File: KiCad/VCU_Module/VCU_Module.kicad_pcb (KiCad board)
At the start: 4 copper layers, 85.2 x 107.8 mm, 66 parts, among them IC1 STM32C092RCT6, J1 5810132011, J10 12V, J11 Conn_ST_STDC14, J12 MCU1, J13 MCU2, J14 5V, J15 3V3, J16 MCU3, J17 MCU4, J2 CN1, J3 CN2, J4 CN3, J5 MCU6, J6 CN4, J7 MCU5, J8 Termination Resistor Jumper, J9 GND, Q1 SUD19P06-60, SW2 SW_Push, U3 LMR33640DDDA, U4 LMR33640DDDA, U6 MCP2562FDT-H_SN

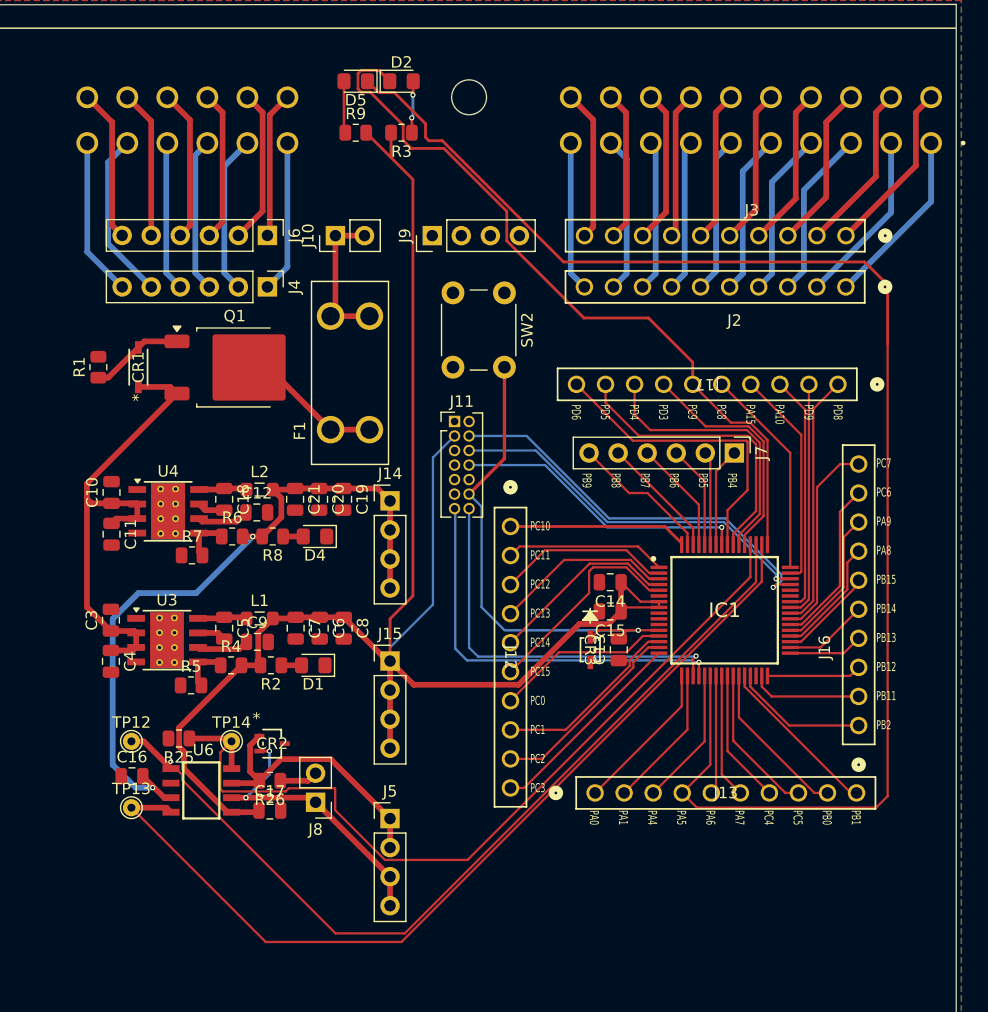
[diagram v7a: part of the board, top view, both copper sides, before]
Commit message: finished DRC checks and ERC checks in schematic and PCB, added many new components with purchase links to BOM, still need to double check previously added parts in BOM to ensure they are sufficient for higher voltage inputs
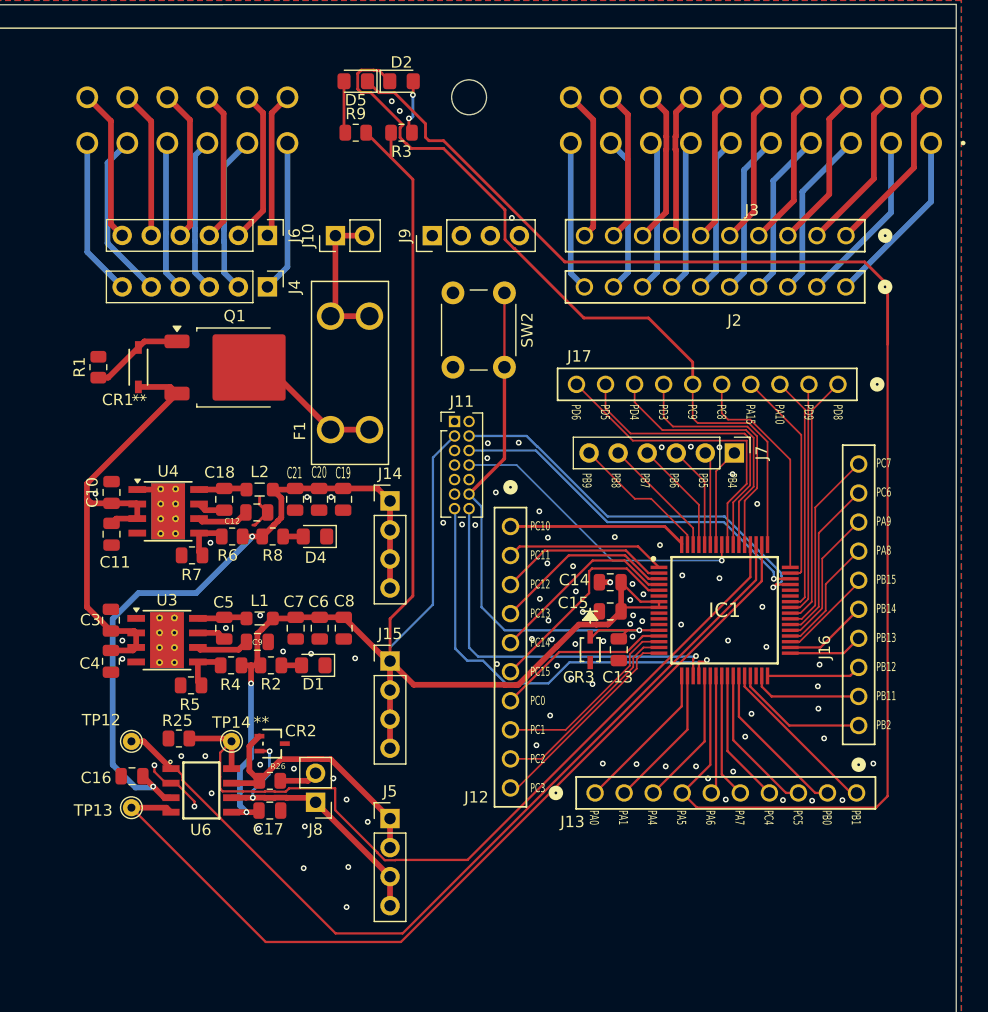
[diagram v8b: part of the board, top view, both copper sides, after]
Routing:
- net GND: track 0.00 -> 12.0 mm, vias 0 -> 92
- net /MCU/NRST: track 44.7 -> 51.2 mm
- net 3V3: track 152.7 -> 149.4 mm, vias 0 -> 2
- net /MCU/VCP_RX: track 35.3 -> 38.4 mm
- net /MCU/PC9/User LED 2: track 65.7 -> 67.7 mm
- net VDD: track 14.4 -> 13.2 mm
- net /MCU/PD3: track 20.5 -> 21.7 mm
- net /MCU/PC8/TIM1_CH1: track 18.5 -> 19.6 mm
- net /MCU/PD4: track 24.3 -> 23.1 mm
- net /MCU/SWO: track 25.9 -> 26.9 mm
- net /MCU/PC7: track 17.5 -> 16.6 mm
